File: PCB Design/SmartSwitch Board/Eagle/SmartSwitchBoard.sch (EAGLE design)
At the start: 13 parts, among them IC1 MCP23017SS

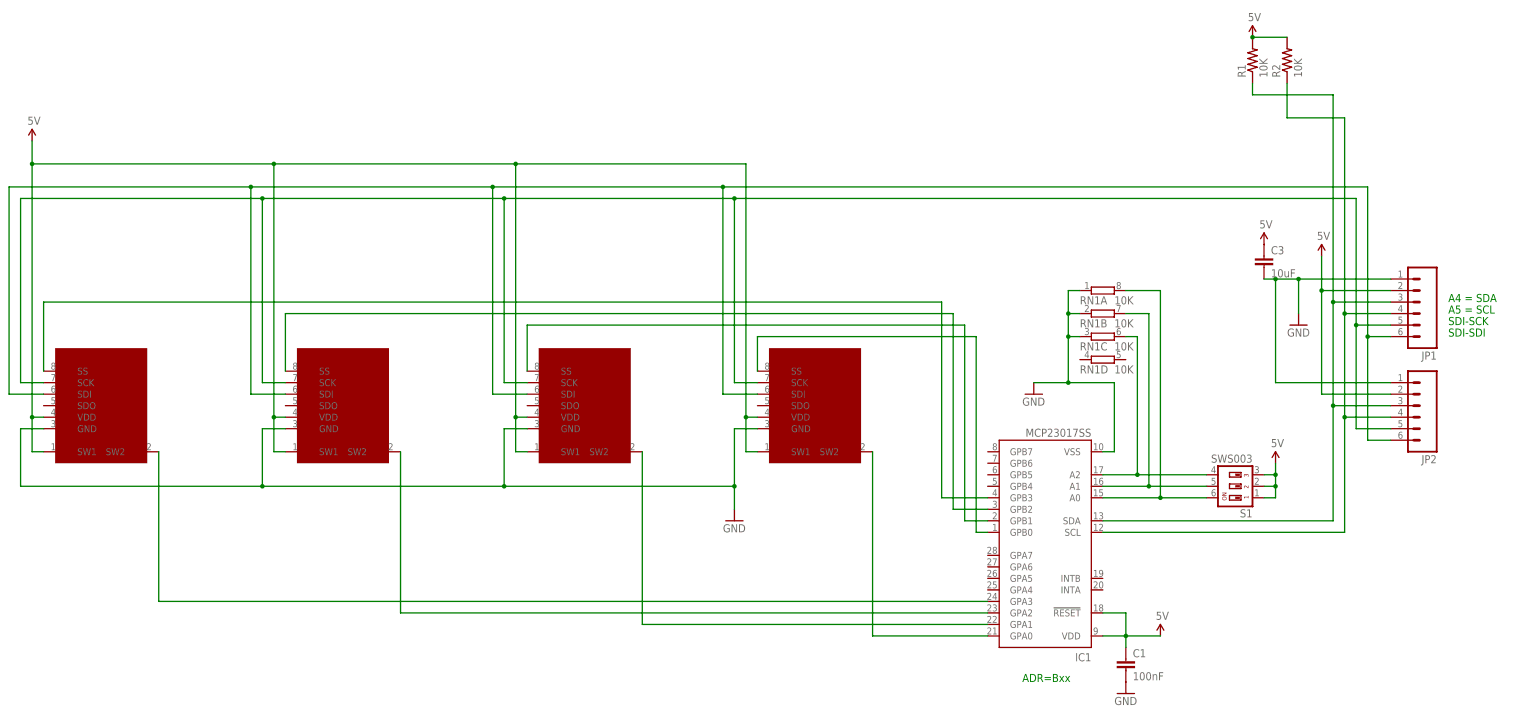
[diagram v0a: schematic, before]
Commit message: Added new header to smartswitch board - still needs routing
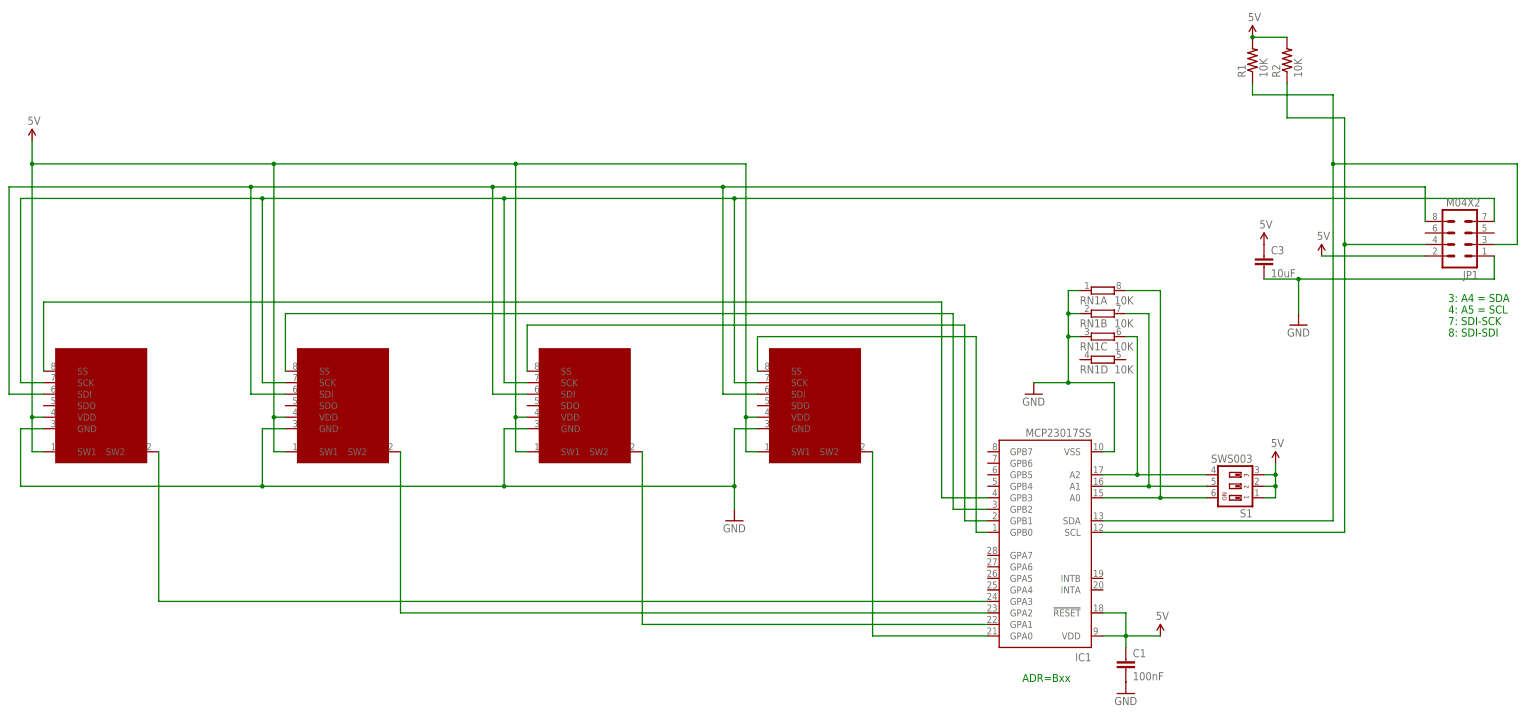
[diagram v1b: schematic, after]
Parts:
- removed JP2: (no value), SparkFun:M06SIP
- JP1: value (none) -> M04X2; device SparkFun:M06SIP -> SparkFun:M04X2
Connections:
- net 5V: no longer JP2.2
- net GND: no longer JP2.1
- net N$3: no longer JP2.3
- net N$6: no longer JP2.4
- net N$7: now also JP1.7; no longer JP1.5, JP2.5
- net N$8: now also JP1.8; no longer JP1.6, JP2.6
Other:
- note added: "3: A4 = SDA"
- note added: "4: A5 = SCL"
- note added: "7: SDI-SCK"
- note added: "8: SDI-SDI"
- note removed: "A4 = SDA"
- note removed: "A5 = SCL"
- note removed: "SDI-SCK"
- note removed: "SDI-SDI"
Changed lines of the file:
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@@
 <part name="U$7" library="SparkFun" deviceset="5V" device=""/>
 <part name="GND3" library="SparkFun" deviceset="GND" device=""/>
-<part name="JP1" library="SparkFun" deviceset="M06" device="SIP"/>
-<part name="JP2" library="SparkFun" deviceset="M06" device="SIP"/>
+<part name="JP1" library="SparkFun" deviceset="M04X2" device=""/>
 <part name="GND1" library="SparkFun" deviceset="GND" device=""/>
 <part name="GND2" library="SparkFun" deviceset="GND" device=""/>
@@
 <sheet>
 <plain>
-<text x="193.04" y="20.32" size="1.778" layer="91">A5 = SCL</text>
-<text x="193.04" y="22.86" size="1.778" layer="91">A4 = SDA</text>
+<text x="193.04" y="20.32" size="1.778" layer="91">4: A5 = SCL</text>
+<text x="193.04" y="22.86" size="1.778" layer="91">3: A4 = SDA</text>
 <text x="99.06" y="-60.96" size="1.778" layer="91">ADR=Bxx</text>
-<text x="193.04" y="17.78" size="1.778" layer="91">SDI-SCK</text>
-<text x="193.04" y="15.24" size="1.778" layer="91">SDI-SDI</text>
+<text x="193.04" y="17.78" size="1.778" layer="91">7: SDI-SCK</text>
+<text x="193.04" y="15.24" size="1.778" layer="91">8: SDI-SDI</text>
 </plain>
 <instances>
@@
 <instance part="U$7" gate="G$1" x="-119.38" y="58.42"/>
 <instance part="GND3" gate="1" x="35.56" y="-25.4"/>
-<instance part="JP1" gate="G$1" x="185.42" y="22.86" rot="R180"/>
-<instance part="JP2" gate="G$1" x="185.42" y="0" rot="R180"/>
+<instance part="JP1" gate="G$1" x="195.58" y="38.1" rot="R180"/>
 <instance part="GND1" gate="1" x="121.92" y="-63.5"/>
 <instance part="GND2" gate="1" x="101.6" y="2.54"/>
@@
 <pinref part="C1" gate="G$1" pin="1"/>
 <wire x1="121.92" y1="-50.8" x2="121.92" y2="-53.34" width="0.1524" layer="91"/>
-</segment>
-<segment>
-<wire x1="180.34" y1="25.4" x2="165.1" y2="25.4" width="0.1524" layer="91"/>
-<wire x1="165.1" y1="25.4" x2="165.1" y2="33.02" width="0.1524" layer="91"/>
-<pinref part="U$12" gate="G$1" pin="5V"/>
-<wire x1="180.34" y1="2.54" x2="165.1" y2="2.54" width="0.1524" layer="91"/>
-<wire x1="165.1" y1="2.54" x2="165.1" y2="25.4" width="0.1524" layer="91"/>
-<junction x="165.1" y="25.4"/>
-<pinref part="JP1" gate="G$1" pin="2"/>
-<pinref part="JP2" gate="G$1" pin="2"/>
 </segment>
 <segment>
@@
 <junction x="38.1" y="-2.54"/>
 </segment>
+<segment>
+<pinref part="U$12" gate="G$1" pin="5V"/>
+<pinref part="JP1" gate="G$1" pin="2"/>
+<wire x1="165.1" y1="33.02" x2="187.96" y2="33.02" width="0.1524" layer="91"/>
+</segment>
 </net>
 <net name="GND" class="1">
 <segment>
-<wire x1="180.34" y1="27.94" x2="160.02" y2="27.94" width="0.1524" layer="91"/>
 <wire x1="160.02" y1="27.94" x2="160.02" y2="20.32" width="0.1524" layer="91"/>
 <pinref part="GND4" gate="1" pin="GND"/>
-<wire x1="180.34" y1="5.08" x2="154.94" y2="5.08" width="0.1524" layer="91"/>
-<wire x1="154.94" y1="5.08" x2="154.94" y2="27.94" width="0.1524" layer="91"/>
-<wire x1="154.94" y1="27.94" x2="160.02" y2="27.94" width="0.1524" layer="91"/>
-<junction x="160.02" y="27.94"/>
-<wire x1="154.94" y1="27.94" x2="152.4" y2="27.94" width="0.1524" layer="91"/>
-<junction x="154.94" y="27.94"/>
+<wire x1="152.4" y1="27.94" x2="160.02" y2="27.94" width="0.1524" layer="91"/>
 <pinref part="C3" gate="G$1" pin="2"/>
 <pinref part="JP1" gate="G$1" pin="1"/>
-<pinref part="JP2" gate="G$1" pin="1"/>
+<wire x1="203.2" y1="33.02" x2="203.2" y2="27.94" width="0.1524" layer="91"/>
+<wire x1="203.2" y1="27.94" x2="160.02" y2="27.94" width="0.1524" layer="91"/>
+<junction x="160.02" y="27.94"/>
 </segment>
 <segment>
@@
 <pinref part="IC1" gate="G$1" pin="SCL"/>
 <wire x1="116.84" y1="-27.94" x2="170.18" y2="-27.94" width="0.1524" layer="91"/>
-<wire x1="170.18" y1="-27.94" x2="170.18" y2="-2.54" width="0.1524" layer="91"/>
-<wire x1="170.18" y1="-2.54" x2="170.18" y2="20.32" width="0.1524" layer="91"/>
-<wire x1="170.18" y1="20.32" x2="180.34" y2="20.32" width="0.1524" layer="91"/>
-<wire x1="170.18" y1="20.32" x2="170.18" y2="63.5" width="0.1524" layer="91"/>
-<junction x="170.18" y="20.32"/>
+<wire x1="170.18" y1="-27.94" x2="170.18" y2="35.56" width="0.1524" layer="91"/>
+<wire x1="170.18" y1="35.56" x2="170.18" y2="63.5" width="0.1524" layer="91"/>
 <wire x1="170.18" y1="63.5" x2="157.48" y2="63.5" width="0.1524" layer="91"/>
-<wire x1="180.34" y1="-2.54" x2="170.18" y2="-2.54" width="0.1524" layer="91"/>
-<junction x="170.18" y="-2.54"/>
 <pinref part="R2" gate="G$1" pin="1"/>
 <wire x1="157.48" y1="71.12" x2="157.48" y2="63.5" width="0.1524" layer="91"/>
 <pinref part="JP1" gate="G$1" pin="4"/>
-<pinref part="JP2" gate="G$1" pin="4"/>
+<wire x1="187.96" y1="35.56" x2="170.18" y2="35.56" width="0.1524" layer="91"/>
+<junction x="170.18" y="35.56"/>
 </segment>
 </net>
@@
 <segment>
 <wire x1="149.86" y1="68.58" x2="167.64" y2="68.58" width="0.1524" layer="91"/>
-<wire x1="167.64" y1="68.58" x2="167.64" y2="22.86" width="0.1524" layer="91"/>
 <pinref part="IC1" gate="G$1" pin="SDA"/>
-<wire x1="167.64" y1="22.86" x2="167.64" y2="0" width="0.1524" layer="91"/>
-<wire x1="167.64" y1="0" x2="167.64" y2="-25.4" width="0.1524" layer="91"/>
+<wire x1="167.64" y1="68.58" x2="167.64" y2="53.34" width="0.1524" layer="91"/>
+<wire x1="167.64" y1="53.34" x2="167.64" y2="-25.4" width="0.1524" layer="91"/>
 <wire x1="167.64" y1="-25.4" x2="116.84" y2="-25.4" width="0.1524" layer="91"/>
-<wire x1="167.64" y1="22.86" x2="180.34" y2="22.86" width="0.1524" layer="91"/>
-<junction x="167.64" y="22.86"/>
-<wire x1="180.34" y1="0" x2="167.64" y2="0" width="0.1524" layer="91"/>
-<junction x="167.64" y="0"/>
 <pinref part="R1" gate="G$1" pin="1"/>
 <wire x1="149.86" y1="71.12" x2="149.86" y2="68.58" width="0.1524" layer="91"/>
 <pinref part="JP1" gate="G$1" pin="3"/>
-<pinref part="JP2" gate="G$1" pin="3"/>
+<wire x1="203.2" y1="35.56" x2="208.28" y2="35.56" width="0.1524" layer="91"/>
+<wire x1="208.28" y1="35.56" x2="208.28" y2="53.34" width="0.1524" layer="91"/>
+<wire x1="208.28" y1="53.34" x2="167.64" y2="53.34" width="0.1524" layer="91"/>
+<junction x="167.64" y="53.34"/>
 </segment>
 </net>
@@
 <net name="N$7" class="0">
 <segment>
-<pinref part="JP2" gate="G$1" pin="5"/>
-<wire x1="180.34" y1="-5.08" x2="172.72" y2="-5.08" width="0.1524" layer="91"/>
-<wire x1="172.72" y1="-5.08" x2="172.72" y2="17.78" width="0.1524" layer="91"/>
-<wire x1="172.72" y1="17.78" x2="172.72" y2="45.72" width="0.1524" layer="91"/>
-<wire x1="172.72" y1="45.72" x2="35.56" y2="45.72" width="0.1524" layer="91"/>
+<wire x1="203.2" y1="45.72" x2="35.56" y2="45.72" width="0.1524" layer="91"/>
 <wire x1="35.56" y1="45.72" x2="-15.24" y2="45.72" width="0.1524" layer="91"/>
 <wire x1="-15.24" y1="45.72" x2="-68.58" y2="45.72" width="0.1524" layer="91"/>
@@
 <pinref part="U$6" gate="G$1" pin="SCK"/>
 <wire x1="-121.92" y1="5.08" x2="-116.84" y2="5.08" width="0.1524" layer="91"/>
-<pinref part="JP1" gate="G$1" pin="5"/>
-<wire x1="172.72" y1="17.78" x2="180.34" y2="17.78" width="0.1524" layer="91"/>
-<junction x="172.72" y="17.78"/>
 <wire x1="-68.58" y1="45.72" x2="-68.58" y2="5.08" width="0.1524" layer="91"/>
 <junction x="-68.58" y="45.72"/>
@@
 <pinref part="U$3" gate="G$1" pin="SCK"/>
 <wire x1="35.56" y1="5.08" x2="40.64" y2="5.08" width="0.1524" layer="91"/>
+<pinref part="JP1" gate="G$1" pin="7"/>
+<wire x1="203.2" y1="45.72" x2="203.2" y2="40.64" width="0.1524" layer="91"/>
 </segment>
 </net>
@@
 <wire x1="-71.12" y1="48.26" x2="-17.78" y2="48.26" width="0.1524" layer="91"/>
 <wire x1="-17.78" y1="48.26" x2="33.02" y2="48.26" width="0.1524" layer="91"/>
-<wire x1="33.02" y1="48.26" x2="175.26" y2="48.26" width="0.1524" layer="91"/>
-<wire x1="175.26" y1="48.26" x2="175.26" y2="15.24" width="0.1524" layer="91"/>
-<pinref part="JP2" gate="G$1" pin="6"/>
-<wire x1="175.26" y1="15.24" x2="175.26" y2="-7.62" width="0.1524" layer="91"/>
-<wire x1="175.26" y1="-7.62" x2="180.34" y2="-7.62" width="0.1524" layer="91"/>
-<pinref part="JP1" gate="G$1" pin="6"/>
-<wire x1="180.34" y1="15.24" x2="175.26" y2="15.24" width="0.1524" layer="91"/>
-<junction x="175.26" y="15.24"/>
+<wire x1="33.02" y1="48.26" x2="187.96" y2="48.26" width="0.1524" layer="91"/>
 <pinref part="U$3" gate="G$1" pin="SDI"/>
 <wire x1="40.64" y1="2.54" x2="33.02" y2="2.54" width="0.1524" layer="91"/>
@@
 <wire x1="-71.12" y1="2.54" x2="-71.12" y2="48.26" width="0.1524" layer="91"/>
 <junction x="-71.12" y="48.26"/>
-</segment>
-</net>
+<pinref part="JP1" gate="G$1" pin="8"/>
+<wire x1="187.96" y1="48.26" x2="187.96" y2="40.64" width="0.1524" layer="91"/>
+</segment>
+</net>
